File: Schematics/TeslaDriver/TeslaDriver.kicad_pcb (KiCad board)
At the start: 2 copper layers, 115 x 50 mm, 57 parts, among them P1 CONTROL, P2 PWR_IN+, P3 PWR_GND, P4 PWR_OUT_L2, P5 PWR_OUT_L1, Q1 STP65NF06, Q2 STP65NF06, Q3 STP65NF06, Q4 STP65NF06, T1 GateTR10x4, T2 GateTR10x4, T3 GateTR10x4, T4 GateTR10x4, U1 DS18B20, U2 DS18B20, U3 UCC27424D, U4 UCC27424D

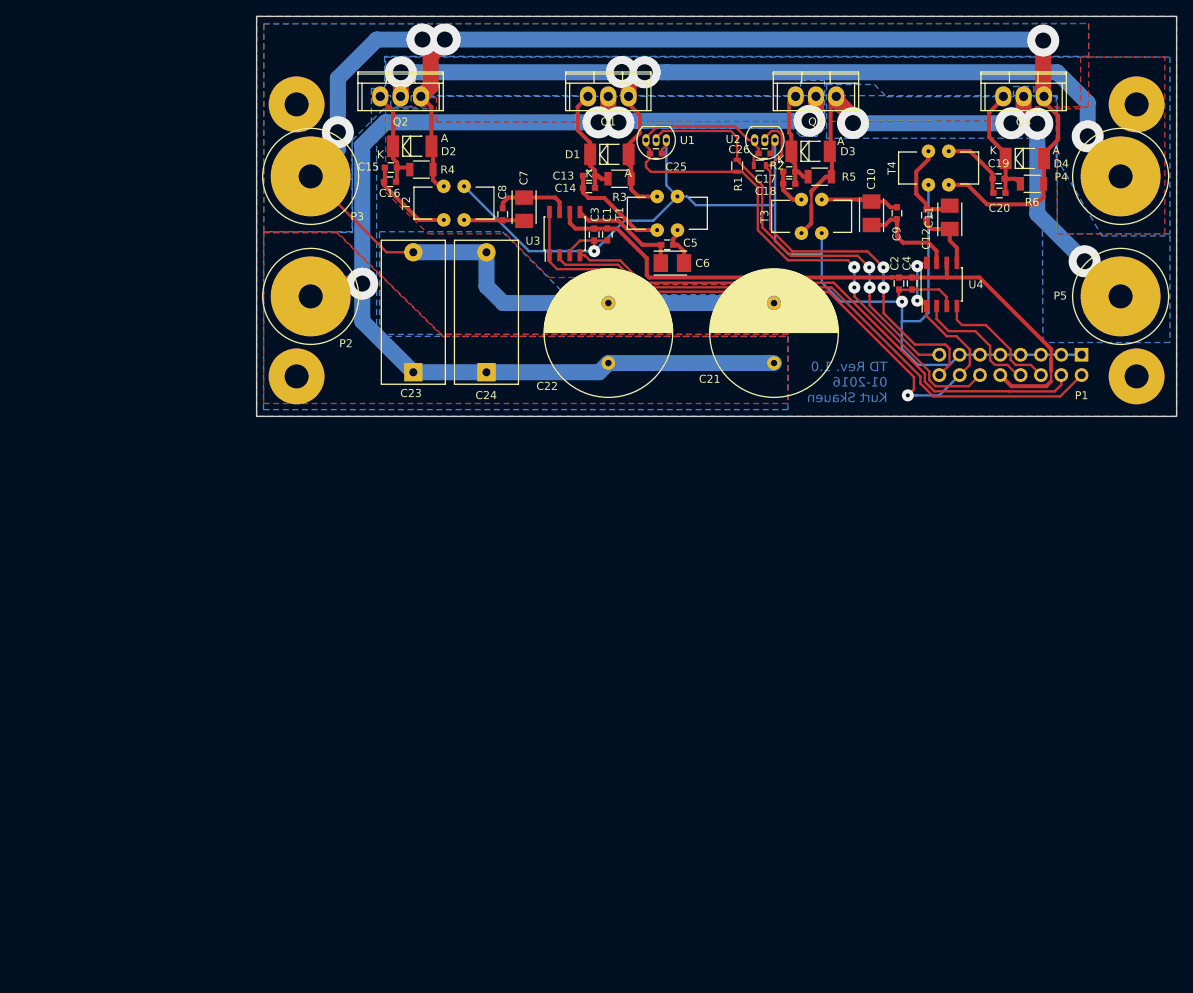
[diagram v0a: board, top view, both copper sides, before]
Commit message: * Redesigned the inverter gate driver. 	- It will now drive the gate to ~+-12V rather than ~-0.6 to 11.4. 	- Redesigned the gate clamping to better enforce the gate voltage 	  limit and to more quickly adapt the gate transformers DC level when 	  changing duty cycle.
* Redesigned the inverter PCB.
	- Made an entirely new layout for the inverter PCB which hopefully
	  will be able to carry substantial currents without needing extra
	  bus bars. It should also give parasitic inductances on the board
	  less oportunity to mess with the GS voltage.
	- Designed for manufacturing on a board-hose rather than home
	  etch.
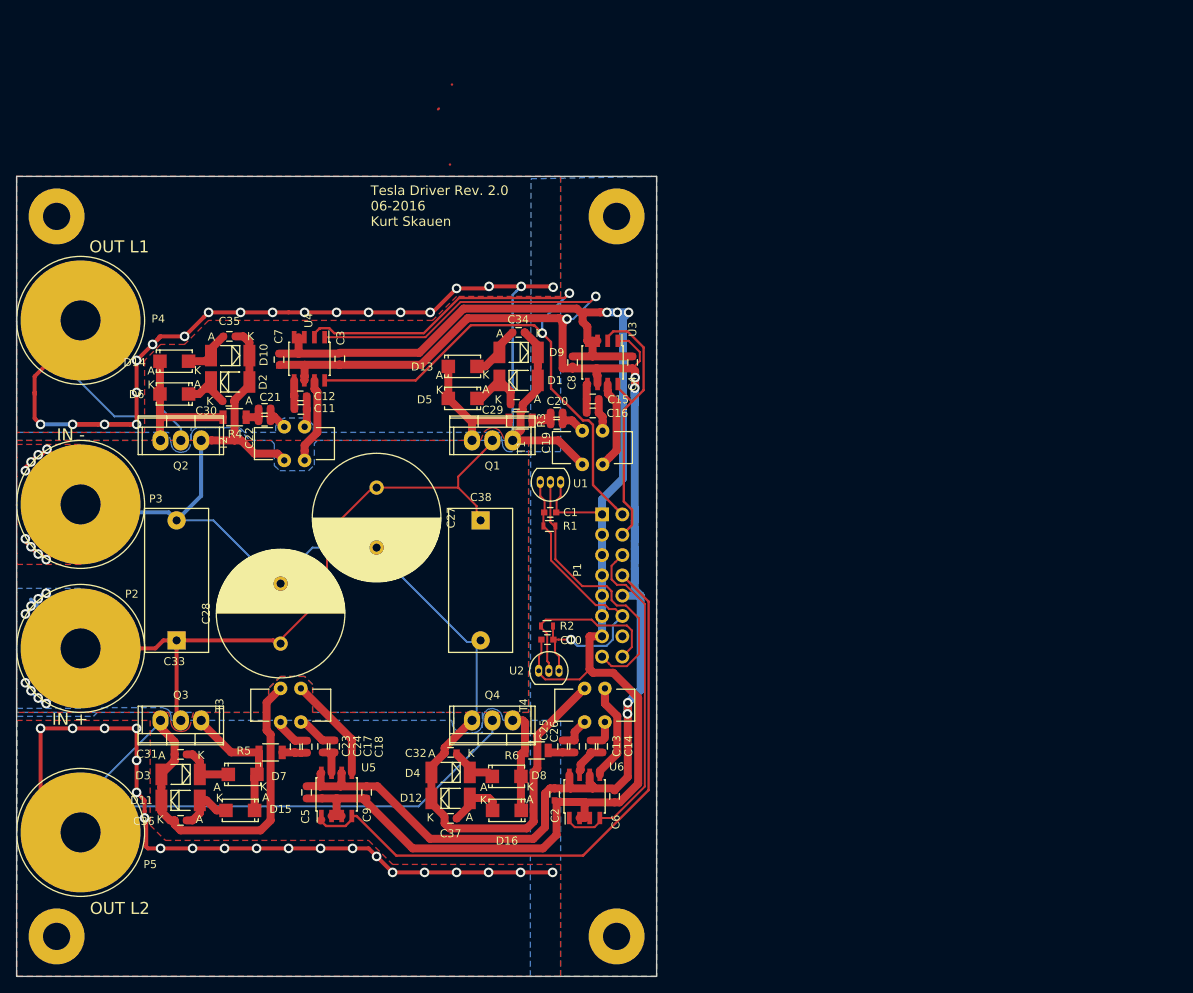
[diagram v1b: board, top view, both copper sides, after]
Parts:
- removed the C10 at (206.9, 54.6)
- removed the C15 at (146.8, 48.9)
- removed the C4 at (211.9, 63.4)
- removed the C8 at (160.8, 54.7)
- removed REF** (x4): MH7x3, MyMechanical:MH7x3
- added C21: 100n, MyCapacitors:C_0603, F.Cu at (131.0, 79.0)
- added C22: 1u, Capacitors_SMD:C_0603, F.Cu at (131.0, 80.6)
- added C23: 100n, MyCapacitors:C_0603, F.Cu at (134.8, 121.3)
- added C24: 1u, Capacitors_SMD:C_0603, F.Cu at (136.3, 121.3)
- added C25: 100n, MyCapacitors:C_0603, F.Cu at (168.2, 121.2)
- added C26: 1u, Capacitors_SMD:C_0603, F.Cu at (169.8, 121.2)
- added C29: 1u, MyCapacitors:C_0603, F.Cu at (162.5, 78.5)
- added C3: 1u, MyCapacitors:C_0603, F.Cu at (140.4, 72.8)
- added C30: 1u, MyCapacitors:C_0603, F.Cu at (126.5, 78.1)
- added C31: 1u, MyCapacitors:C_0603, F.Cu at (120.5, 122.2)
- added C32: 1u, MyCapacitors:C_0603, F.Cu at (154.2, 122.0)
- added C34: 1u, MyCapacitors:C_0603, F.Cu at (162.8, 69.5)
- added C35: 1u, MyCapacitors:C_0603, F.Cu at (126.6, 70.0)
- added C36: 1u, MyCapacitors:C_0603, F.Cu at (120.5, 130.5)
- added C37: 1u, MyCapacitors:C_0603, F.Cu at (154.2, 130.2)
- added C5: 1u, MyCapacitors:C_0603, F.Cu at (136.2, 127.0)
- added D10: ZMY12, MyDiodes:MELF_Standard, F.Cu at (126.7, 72.4)
- added D11: ZMY12, MyDiodes:MELF_Standard, F.Cu at (120.5, 128.0)
- added D12: ZMY12, MyDiodes:MELF_Standard, F.Cu at (154.2, 127.8)
- added D13: SS210, MyDiodes:Diode-SMA_Standard, F.Cu at (155.8, 73.8)
- added D14: SS210, MyDiodes:Diode-SMA_Standard, F.Cu at (119.7, 73.1)
- added D15: SS210, MyDiodes:Diode-SMA_Standard, F.Cu at (128.0, 129.2)
- added D16: SS210, MyDiodes:Diode-SMA_Standard, F.Cu at (161.3, 129.2)
- added D5: SS210, MyDiodes:Diode-SMA_Standard, F.Cu at (155.8, 77.8)
- added D6: SS210, MyDiodes:Diode-SMA_Standard, F.Cu at (119.7, 77.2)
- added D7: SS210, MyDiodes:Diode-SMA_Standard, F.Cu at (128.2, 124.8)
- added D8: SS210, MyDiodes:Diode-SMA_Standard, F.Cu at (161.2, 125.0)
- added D9: ZMY12, MyDiodes:MELF_Standard, F.Cu at (162.8, 72.0)
- added M1: MountingHole, MyMechanical:MH7x3, F.Cu at (105.0, 55.0)
- added M2: MountingHole, MyMechanical:MH7x3, F.Cu at (105.0, 145.0)
- added M3: MountingHole, MyMechanical:MH7x3, F.Cu at (175.0, 55.0)
- added M4: MountingHole, MyMechanical:MH7x3, F.Cu at (175.0, 145.0)
- added U5: NCP81071A, MyFootprints:SOIC-8_3.9x4.9mm_Pitch1.27mm, F.Cu at (140.0, 127.2)
- added U6: NCP81071A, MyFootprints:SOIC-8_3.9x4.9mm_Pitch1.27mm, F.Cu at (171.0, 127.5)
- C11, C6, C7: value 10u -> 100n; footprint Capacitors_Tantalum_SMD:TantalC_SizeB_EIA-3528_Reflow -> MyCapacitors:C_0603
- C12: value 100n -> 1u
- C14, C16, C18: footprint Capacitors_SMD:C_0603 -> MyCapacitors:C_0603
- P2, P3: footprint MyConnectors:PowerPad10 -> MyConnectors:PowerPad15_5
- P4: value PWR_OUT_L2 -> PWR_OUT_L1; footprint MyConnectors:PowerPad10 -> MyConnectors:PowerPad15_5
- P5: value PWR_OUT_L1 -> PWR_OUT_L2; footprint MyConnectors:PowerPad10 -> MyConnectors:PowerPad15_5
- R3, R4, R5, R6: value 150R -> 2
- U3, U4: value UCC27424D -> NCP81071A
- moved P5 146.2 mm to (108.0, 132.0)
- moved P4 131.2 mm to (108.0, 68.0)
- moved Q3 111.3 mm to (120.5, 118.0), turned to 180 degrees
- moved D3 110.8 mm to (120.5, 124.8), turned to 180 degrees
- moved D4 105.1 mm to (154.2, 124.5), turned to 180 degrees
- moved Q4 102.4 mm to (159.5, 118.0), turned to 180 degrees
- moved R5 99.4 mm to (131.8, 122.0)
- moved C9 98.2 mm to (143.8, 127.0), turned to 270 degrees
- moved R6 94.1 mm to (165.0, 121.8)
- moved C17 92.5 mm to (138.2, 121.2), turned to 90 degrees
- moved C18 90.4 mm to (139.8, 121.2), turned to 90 degrees
- moved T3 89.3 mm to (135.5, 116.1)
- moved C11 84.6 mm to (135.5, 79.1), turned to 0 degrees
- moved C12 81.4 mm to (135.5, 77.4), turned to 0 degrees
- moved U4 79.6 mm to (136.6, 72.8), turned to 270 degrees
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- renumbered C25 to C1, C26 to C10, C5 to C15, C21 to C27, C22 to C28, C23 to C33, C24 to C38, C1 to C4, C3 to C8
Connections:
- C14 pad 1: Net-(C13-Pad2) -> Net-(C13-Pad1)
- C14 pad 2: Net-(C13-Pad1) -> Net-(C13-Pad2)
- C15 pad 1: Net-(C5-Pad1) -> Net-(C15-Pad1)
- C15 pad 2: Net-(C5-Pad2) -> Net-(C15-Pad2)
- C16 pad 1: Net-(C15-Pad2) -> Net-(C15-Pad1)
- C16 pad 2: Net-(C15-Pad1) -> Net-(C15-Pad2)
- C18 pad 1: Net-(C17-Pad2) -> Net-(C17-Pad1)
- C18 pad 2: Net-(C17-Pad1) -> Net-(C17-Pad2)
- C6 pad 1: Net-(C5-Pad1) -> +12V
- C6 pad 2: Net-(C5-Pad2) -> GND
- C7 pad 1: Net-(C7-Pad1) -> +12V
- C7 pad 2: Net-(C7-Pad2) -> GND
- C9 pad 1: Net-(C10-Pad1) -> +12V
- C9 pad 2: Net-(C10-Pad2) -> GND
- D1 pad 1: Net-(C13-Pad2) -> Net-(C29-Pad1)
- D1 pad 2: /OUTL2 -> /OUTL1
- D2 pad 1: Net-(C15-Pad2) -> Net-(C30-Pad1)
- D3 pad 1: Net-(C17-Pad2) -> Net-(C31-Pad1)
- D3 pad 2: /OUTL1 -> /OUTL2
- D4 pad 1: Net-(C19-Pad2) -> Net-(C32-Pad1)
- P1 pad 14: /GateEnable -> (no net)
- P4 pad 1: /OUTL2 -> /OUTL1
- P5 pad 1: /OUTL1 -> /OUTL2
- Q1 pad 1: Net-(C13-Pad2) -> Net-(D13-Pad1)
- Q1 pad 3: /OUTL2 -> /OUTL1
- Q2 pad 1: Net-(C15-Pad2) -> Net-(D14-Pad1)
- Q2 pad 2: /OUTL2 -> /OUTL1
- Q3 pad 1: Net-(C17-Pad2) -> Net-(D15-Pad1)
- Q3 pad 3: /OUTL1 -> /OUTL2
- Q4 pad 1: Net-(C19-Pad2) -> Net-(D16-Pad1)
- Q4 pad 2: /OUTL1 -> /OUTL2
- R3 pad 1: /OUTL2 -> Net-(C19-Pad2)
- R3 pad 2: Net-(C13-Pad2) -> Net-(D13-Pad1)
- R4 pad 1: GNDPWR -> Net-(C21-Pad2)
- R4 pad 2: Net-(C15-Pad2) -> Net-(D14-Pad1)
- R5 pad 1: /OUTL1 -> Net-(C23-Pad2)
- R5 pad 2: Net-(C17-Pad2) -> Net-(D15-Pad1)
- R6 pad 1: GNDPWR -> Net-(C25-Pad2)
- R6 pad 2: Net-(C19-Pad2) -> Net-(D16-Pad1)
- T1 pad 1: GND -> Net-(C15-Pad2)
- T1 pad 2: Net-(C5-Pad2) -> Net-(T1-Pad2)
- T1 pad 3: /OUTL2 -> Net-(C19-Pad1)
- T1 pad 4: Net-(C13-Pad1) -> /OUTL1
- T2 pad 1: GND -> Net-(C11-Pad2)
- T2 pad 2: Net-(C7-Pad2) -> Net-(T2-Pad2)
- T2 pad 3: GNDPWR -> Net-(C21-Pad1)
- T2 pad 4: Net-(C15-Pad1) -> GNDPWR
- T3 pad 1: Net-(C10-Pad2) -> Net-(T3-Pad1)
- T3 pad 2: GND -> Net-(C17-Pad2)
- T3 pad 3: Net-(C17-Pad1) -> /OUTL2
- T3 pad 4: /OUTL1 -> Net-(C23-Pad1)
- T4 pad 1: GND -> Net-(T4-Pad1)
- T4 pad 2: Net-(C11-Pad2) -> Net-(C13-Pad2)
- T4 pad 4: Net-(C19-Pad1) -> Net-(C25-Pad1)
- U3 pad 1: /GateEnable -> +12V
- U3 pad 2: /GatePWM1L -> /GatePWM1H
- U3 pad 4: /GatePWM1H -> GND
- U3 pad 5: Net-(C5-Pad1) -> Net-(C15-Pad1)
- U3 pad 7: Net-(C7-Pad1) -> Net-(T1-Pad2)
- U3 pad 8: /GateEnable -> /GatePWM1H
- U4 pad 1: /GateEnable -> +12V
- U4 pad 2: /GatePWM2H -> /GatePWM1L
- U4 pad 4: /GatePWM2L -> GND
- U4 pad 7: Net-(C10-Pad1) -> Net-(T2-Pad2)
- U4 pad 8: /GateEnable -> /GatePWM1L
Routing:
- net +12V: track 83.5 -> 223.3 mm, vias 0 -> 6
- net /OUTL2: track 124.4 -> 213.7 mm, vias 4 -> 21
- net /GateEnable: track 87.0 -> 0.00 mm, vias 3 -> 0
- net /OUTL1: track 79.6 -> 161.5 mm, vias 4 -> 20
- net /GatePWM2H: track 16.1 -> 76.3 mm
- net GND: track 159.4 -> 209.5 mm, vias 2 -> 3
- net GNDPWR: track 233.5 -> 188.2 mm, vias 4 -> 8
- net +3V3: track 83.4 -> 39.7 mm, vias 2 -> 1
- net /GatePWM1H: track 69.4 -> 34.4 mm
- net TEMP_MOSFET2: track 51.9 -> 22.1 mm, vias 2 -> 0
- net /GatePWM2L: track 15.9 -> 44.4 mm
- net /GatePWM1L: track 74.5 -> 99.5 mm, vias 0 -> 2
- net +24V: track 147.5 -> 125.3 mm, vias 4 -> 8
- net TEMP_MOSFET1: track 55.5 -> 34.4 mm, vias 2 -> 0
- net Net-(D14-Pad1): track 0.00 -> 17.9 mm
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- added copper zone on F.Cu, net /OUTL1
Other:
- board size 115 x 50 mm -> 80 x 100 mm
- net class BusBar: clearance 0.25 -> 0.2
- net class Default: clearance 0.25 -> 0.2; via_dia 1.5 -> 1.2; via_drill 0.5 -> 0.7
- net class GateDrive: clearance 0.25 -> 0.2; trace_width 0.5 -> 1; via_dia 1.5 -> 1.2; via_drill 0.5 -> 0.7
- rule pad_to_mask_clearance: 0 -> 0.13
- rule trace_clearance: 0.25 -> 0.2
- rule trace_min: 0.3 -> 0.2
- rule via_min_drill: 0.5 -> 0.7
- rule via_min_size: 1.5 -> 1.2
- board text added: "IN +"
- board text added: "IN -"
- board text added: "OUT L1"
- board text added: "OUT L2"
- board text added: "Tesla Driver Rev. 2.0 06-2016 Kurt Skauen"
- board text removed: "TD Rev. 1.0 01-2016 Kurt Skauen"

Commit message: Did some small component value tweeks and sorted the BOM.
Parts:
- C29, C30, C31, C32, C34, C35, C36, C37: value 1u -> 100n
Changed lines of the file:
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@@
     (links 160)
     (no_connects 0)
-    (area 99.699999 38.166514 182.135 150.42)
+    (area 99.949999 49.949999 180.050001 150.050001)
     (thickness 1.6)
     (drawings 9)
@@
   )
   (setup
-    (last_trace_width 0.5)
+    (last_trace_width 0.3)
     (user_trace_width 0.25)
     (user_trace_width 0.5)
@@
       (effects (font (size 1 1) (thickness 0.15)))
     )
-    (fp_text value 1u (at 0 1.9) (layer F.Fab) hide
+    (fp_text value 100n (at 0 1.9) (layer F.Fab) hide
       (effects (font (size 1 1) (thickness 0.15)))
     )
@@
       (effects (font (size 1 1) (thickness 0.15)))
     )
-    (fp_text value 1u (at 0 1.9) (layer F.Fab)
+    (fp_text value 100n (at 0 1.9) (layer F.Fab)
       (effects (font (size 1 1) (thickness 0.15)))
     )
@@
       (effects (font (size 1 1) (thickness 0.15)))
     )
-    (fp_text value 1u (at 0 1.9 180) (layer F.Fab)
+    (fp_text value 100n (at 0 1.9 180) (layer F.Fab)
       (effects (font (size 1 1) (thickness 0.15)))
     )
@@
       (effects (font (size 1 1) (thickness 0.15)))
     )
-    (fp_text value 1u (at 0 1.9 180) (layer F.Fab)
+    (fp_text value 100n (at 0 1.9 180) (layer F.Fab)
       (effects (font (size 1 1) (thickness 0.15)))
     )
@@
       (effects (font (size 1 1) (thickness 0.15)))
     )
-    (fp_text value 1u (at 0 1.9) (layer F.Fab) hide
+    (fp_text value 100n (at 0 1.9) (layer F.Fab) hide
       (effects (font (size 1 1) (thickness 0.15)))
     )
@@
       (effects (font (size 1 1) (thickness 0.15)))
     )
-    (fp_text value 1u (at 0 1.9) (layer F.Fab)
+    (fp_text value 100n (at 0 1.9) (layer F.Fab)
       (effects (font (size 1 1) (thickness 0.15)))
     )
@@
       (effects (font (size 1 1) (thickness 0.15)))
     )
-    (fp_text value 1u (at 0 1.9 180) (layer F.Fab)
+    (fp_text value 100n (at 0 1.9 180) (layer F.Fab)
       (effects (font (size 1 1) (thickness 0.15)))
     )
@@
       (effects (font (size 1 1) (thickness 0.15)))
     )
-    (fp_text value 1u (at 0 1.9 180) (layer F.Fab)
-      (effects (font (size 1 1) (thickness 0.15)))
-    )
+    (fp_text value 100n (at 0 1.9 180) (layer F.Fab)
+      (effects (font (size 1 1) (thickness 0.15)))
+    )
